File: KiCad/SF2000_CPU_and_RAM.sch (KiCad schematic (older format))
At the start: 6 parts, among them U10 IS61WV20488FBLL-10TLI, U11 IS61WV20488FBLL-10TLI, U12 IS61WV20488FBLL-10TLI, U13 IS61WV20488FBLL-10TLI, U9 68000D

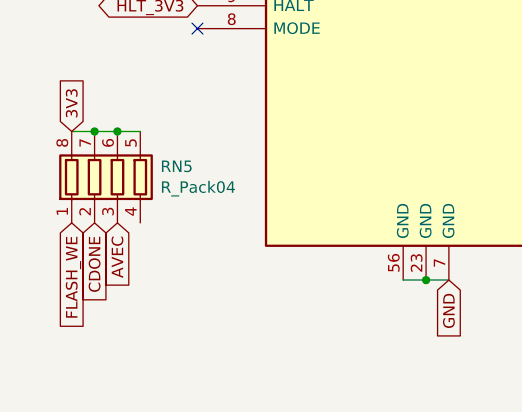
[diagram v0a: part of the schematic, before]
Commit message: Remove IDE-header, add Clockport-header, fixed routing of AVEC and FLASH_OE signals and pull-ups
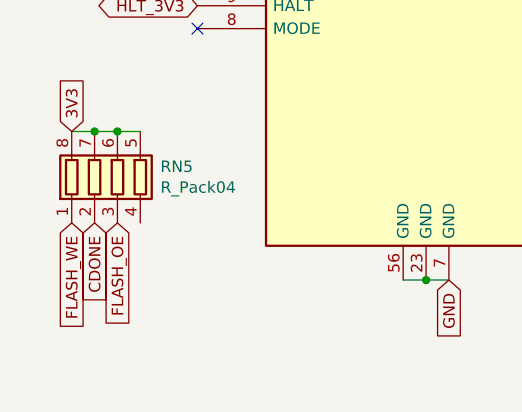
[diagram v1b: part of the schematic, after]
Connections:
- net AVEC: no longer RN5.3 (R3.1)
- new net FLASH_OE: RN5.3 (R3.1)
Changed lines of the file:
@@
 Comment4 ""
 $EndDescr
-$Comp
-L SF2000:68SEC000 U9
-U 1 1 621E09D7
-P 2500 3700
-F 0 "U9" H 2500 3800 50  0000 C CNN
-F 1 "68000D" H 2500 3700 50  0000 C CNN
-F 2 "SF2000:QFP-64_14x14mm_Pitch0.8mm" H 2500 3700 50  0001 C CNN
-F 3 "https://www.nxp.com/docs/en/reference-manual/MC68000UM.pdf" H 2500 3700 50  0001 C CNN
-	1    2500 3700
-	1    0    0    -1
-$EndComp
 Text GLabel 1500 1500 0    50   Input ~ 0
 CLKCPU
@@
 Text GLabel 2600 6100 3    50   Input ~ 0
 GND
-Wire Wire Line
-	2400 6100 2500 6100
-Connection ~ 2500 6100
-Wire Wire Line
-	2500 6100 2600 6100
 Text GLabel 3500 5600 2    50   Output ~ 0
 AS_CPU_3V3
@@
 Text GLabel 1500 4700 0    50   Input ~ 0
 AVEC
-Text GLabel 1150 5850 3    50   Input ~ 0
-AVEC
 Text GLabel 1050 5850 3    50   Input ~ 0
 CDONE
@@
 FLASH_WE
 NoConn ~ 1500 5000
+Wire Wire Line
+	2500 6100 2600 6100
+Wire Wire Line
+	2400 6100 2500 6100
+Connection ~ 2500 6100
+$Comp
+L SF2000:68SEC000 U9
+U 1 1 621E09D7
+P 2500 3700
+F 0 "U9" H 2500 3800 50  0000 C CNN
+F 1 "68000D" H 2500 3700 50  0000 C CNN
+F 2 "SF2000:QFP-64_14x14mm_Pitch0.8mm" H 2500 3700 50  0001 C CNN
+F 3 "https://www.nxp.com/docs/en/reference-manual/MC68000UM.pdf" H 2500 3700 50  0001 C CNN
+	1    2500 3700
+	1    0    0    -1
+$EndComp
+Text GLabel 1150 5850 3    50   Input ~ 0
+FLASH_OE
 $EndSCHEMATC

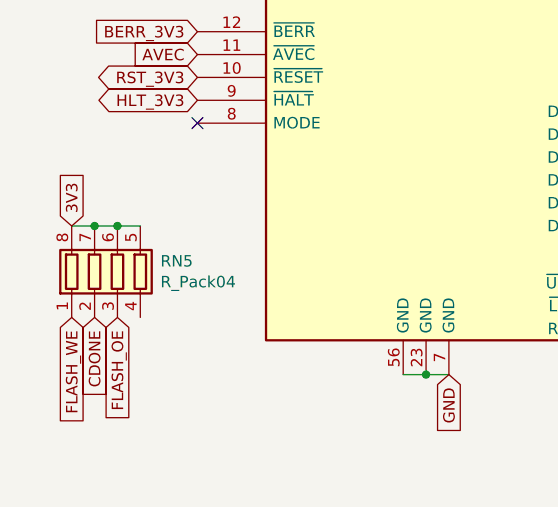
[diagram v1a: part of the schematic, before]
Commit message: Add INT6 signal, Move RN5 to SF2000_FPGA sheet
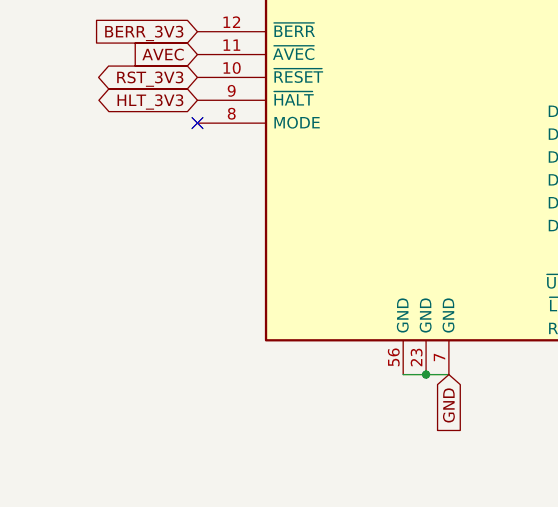
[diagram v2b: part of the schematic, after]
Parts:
- removed RN5: R_Pack04, SF2000:RESCAF80P320X160X60-8N, symbol Device:R_Pack04
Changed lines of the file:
@@
 Text GLabel 3500 5900 2    50   Output ~ 0
 RW_3V3
-Text GLabel 950  5450 1    50   Input ~ 0
-3V3
 $Comp
 L SF2000:IS61WV20488FBLL-10TLI U13
@@
 A21_3V3
 NoConn ~ 3500 1500
-$Comp
-L Device:R_Pack04 RN?
-U 1 1 62C74D68
-P 1150 5650
-AR Path="/62892CF3/62C74D68" Ref="RN?"  Part="1"
-AR Path="/621DFEC4/62C74D68" Ref="RN5"  Part="1"
-F 0 "RN5" H 1338 5696 50  0000 L CNN
-F 1 "R_Pack04" H 1338 5605 50  0000 L CNN
-F 2 "SF2000:RESCAF80P320X160X60-8N" V 1425 5650 50  0001 C CNN
-F 3 "~" H 1150 5650 50  0001 C CNN
-	1    1150 5650
-	1    0    0    -1
-$EndComp
-Wire Wire Line
-	950  5450 1050 5450
-Connection ~ 1050 5450
-Wire Wire Line
-	1050 5450 1150 5450
-Connection ~ 1150 5450
-Wire Wire Line
-	1150 5450 1250 5450
 Text GLabel 1500 4700 0    50   Input ~ 0
 AVEC
-Text GLabel 1050 5850 3    50   Input ~ 0
-CDONE
-Text GLabel 950  5850 3    50   Input ~ 0
-FLASH_WE
 NoConn ~ 1500 5000
 Wire Wire Line
@@
 	1    0    0    -1
 $EndComp
-Text GLabel 1150 5850 3    50   Input ~ 0
-FLASH_OE
 $EndSCHEMATC

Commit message: Fix continuous enumeration for voltage regulators and integrated circuits (U1 to U17)
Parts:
- renumbered U9 to U10, U11 to U14, U10 to U15, U13 to U16, U12 to U17
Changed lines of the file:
@@
 RW_3V3
 $Comp
-L SF2000:IS61WV20488FBLL-10TLI U13
+L SF2000:IS61WV20488FBLL-10TLI U16
 U 1 1 61F186AC
 P 5450 2100
-F 0 "U13" H 5450 2800 50  0000 C CNN
+F 0 "U16" H 5450 2800 50  0000 C CNN
 F 1 "IS61WV20488FBLL-10TLI" V 5450 2100 50  0000 C CNN
 F 2 "Package_SO:TSOP-II-44_10.16x18.41mm_P0.8mm" H 4950 3250 50  0001 C CNN
@@
 $EndComp
 $Comp
-L SF2000:IS61WV20488FBLL-10TLI U12
+L SF2000:IS61WV20488FBLL-10TLI U17
 U 1 1 61F2712B
 P 8100 2100
-F 0 "U12" H 8100 2800 50  0000 C CNN
+F 0 "U17" H 8100 2800 50  0000 C CNN
 F 1 "IS61WV20488FBLL-10TLI" V 8100 2100 50  0000 C CNN
 F 2 "Package_SO:TSOP-II-44_10.16x18.41mm_P0.8mm" H 7600 3250 50  0001 C CNN
@@
 $EndComp
 $Comp
-L SF2000:IS61WV20488FBLL-10TLI U11
+L SF2000:IS61WV20488FBLL-10TLI U14
 U 1 1 61F2A268
 P 5450 5000
-F 0 "U11" H 5450 5700 50  0000 C CNN
+F 0 "U14" H 5450 5700 50  0000 C CNN
 F 1 "IS61WV20488FBLL-10TLI" V 5450 5000 50  0000 C CNN
 F 2 "Package_SO:TSOP-II-44_10.16x18.41mm_P0.8mm" H 4950 6150 50  0001 C CNN
@@
 $EndComp
 $Comp
-L SF2000:IS61WV20488FBLL-10TLI U10
+L SF2000:IS61WV20488FBLL-10TLI U15
 U 1 1 61F2A272
 P 8100 5000
-F 0 "U10" H 8100 5700 50  0000 C CNN
+F 0 "U15" H 8100 5700 50  0000 C CNN
 F 1 "IS61WV20488FBLL-10TLI" V 8100 5000 50  0000 C CNN
 F 2 "Package_SO:TSOP-II-44_10.16x18.41mm_P0.8mm" H 7600 6150 50  0001 C CNN
@@
 Connection ~ 2500 6100
 $Comp
-L SF2000:68SEC000 U9
+L SF2000:68SEC000 U10
 U 1 1 621E09D7
 P 2500 3700
-F 0 "U9" H 2500 3800 50  0000 C CNN
+F 0 "U10" H 2500 3800 50  0000 C CNN
 F 1 "68000D" H 2500 3700 50  0000 C CNN
 F 2 "SF2000:QFP-64_14x14mm_Pitch0.8mm" H 2500 3700 50  0001 C CNN

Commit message: Remove SRAM footprints (U16, U17) and repurpose pin 123 (WE_BANK1_EVEN) for /INT6 signal
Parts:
- removed U16, U17: IS61WV20488FBLL-10TLI, Package_SO:TSOP-II-44_10.16x18.41mm_P0.8mm, symbol SF2000:IS61WV20488FBLL-10TLI
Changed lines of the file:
@@
 RW_3V3
-$Comp
-L SF2000:IS61WV20488FBLL-10TLI U16
-U 1 1 61F186AC
-P 5450 2100
-F 0 "U16" H 5450 2800 50  0000 C CNN
-F 1 "IS61WV20488FBLL-10TLI" V 5450 2100 50  0000 C CNN
-F 2 "Package_SO:TSOP-II-44_10.16x18.41mm_P0.8mm" H 4950 3250 50  0001 C CNN
-F 3 "https://www.mouser.se/datasheet/2/198/61-64WV20488FALL-FBLL-1518520.pdf" H 5450 2100 50  0001 C CNN
-	1    5450 2100
-	1    0    0    -1
-$EndComp
-$Comp
-L SF2000:IS61WV20488FBLL-10TLI U17
-U 1 1 61F2712B
-P 8100 2100
-F 0 "U17" H 8100 2800 50  0000 C CNN
-F 1 "IS61WV20488FBLL-10TLI" V 8100 2100 50  0000 C CNN
-F 2 "Package_SO:TSOP-II-44_10.16x18.41mm_P0.8mm" H 7600 3250 50  0001 C CNN
-F 3 "https://www.mouser.se/datasheet/2/198/61-64WV20488FALL-FBLL-1518520.pdf" H 8100 2100 50  0001 C CNN
-	1    8100 2100
-	1    0    0    -1
-$EndComp
 $Comp
 L SF2000:IS61WV20488FBLL-10TLI U14

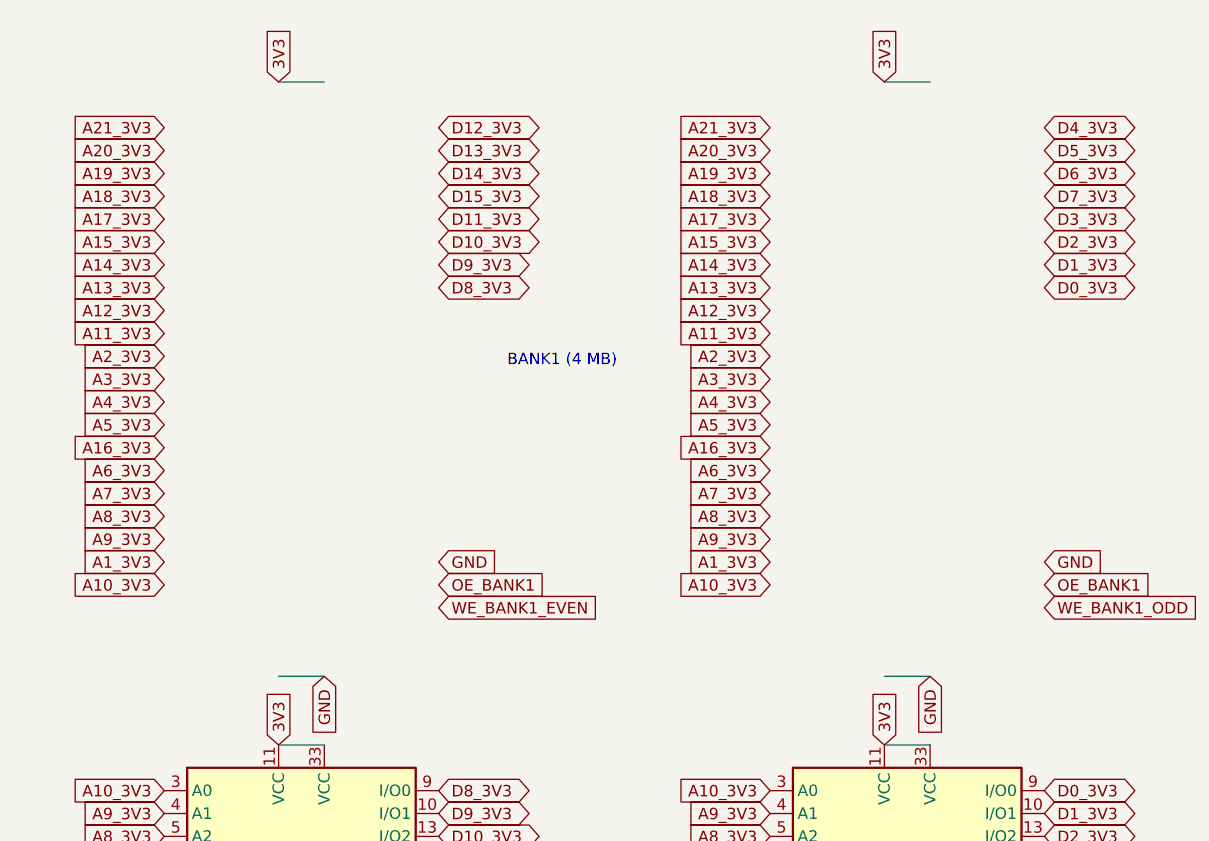
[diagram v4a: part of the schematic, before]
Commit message: Add back SRAM footprints on underside U16,U17
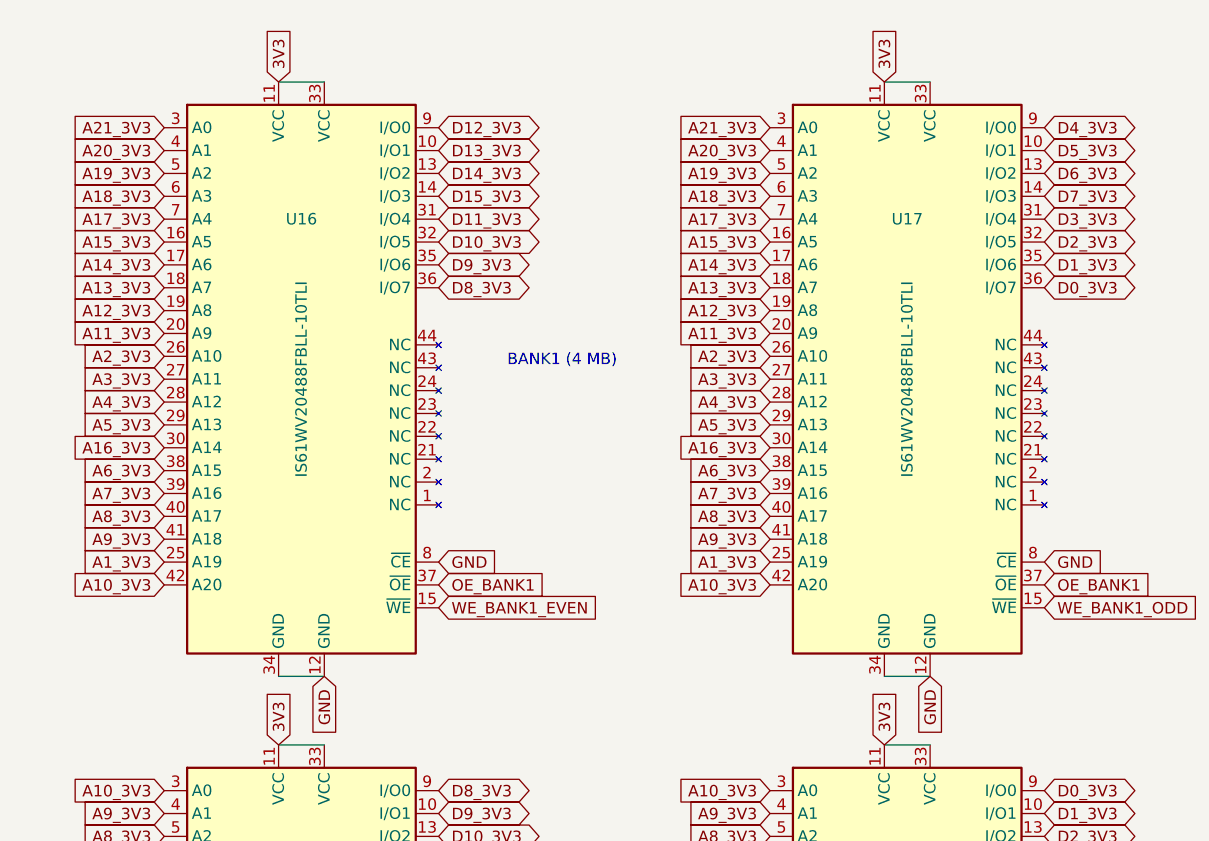
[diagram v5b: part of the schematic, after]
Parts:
- added U16, U17: IS61WV20488FBLL-10TLI, Package_SO:TSOP-II-44_10.16x18.41mm_P0.8mm, symbol SF2000:IS61WV20488FBLL-10TLI
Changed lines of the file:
@@
+	1    0    0    -1
+$EndComp
+$Comp
+L SF2000:IS61WV20488FBLL-10TLI U16
+U 1 1 688516BE
+P 5450 2100
+F 0 "U16" H 5450 2800 50  0000 C CNN
+F 1 "IS61WV20488FBLL-10TLI" V 5450 2100 50  0000 C CNN
+F 2 "Package_SO:TSOP-II-44_10.16x18.41mm_P0.8mm" H 4950 3250 50  0001 C CNN
+F 3 "https://www.mouser.se/datasheet/2/198/61-64WV20488FALL-FBLL-1518520.pdf" H 5450 2100 50  0001 C CNN
+	1    5450 2100
+	1    0    0    -1
+$EndComp
+$Comp
+L SF2000:IS61WV20488FBLL-10TLI U17
+U 1 1 6885F08A
+P 8100 2100
+F 0 "U17" H 8100 2800 50  0000 C CNN
+F 1 "IS61WV20488FBLL-10TLI" V 8100 2100 50  0000 C CNN
+F 2 "Package_SO:TSOP-II-44_10.16x18.41mm_P0.8mm" H 7600 3250 50  0001 C CNN
+F 3 "https://www.mouser.se/datasheet/2/198/61-64WV20488FALL-FBLL-1518520.pdf" H 8100 2100 50  0001 C CNN
+	1    8100 2100
 	1    0    0    -1
 $EndComp
